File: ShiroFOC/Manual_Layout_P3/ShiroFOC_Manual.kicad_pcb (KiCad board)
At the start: 6 copper layers, 45 x 45 mm, 266 parts, among them J1 Motor phases - solder wires, J1001 TC2030-NL SWD, J101 DC input - solder wires, J201 USB-C service, J501 BRAKE RESISTOR, J502 5V PWM FAN, J601 EXT ENCODER / HALL, J801 CAN 1, J802 CAN 2, Q201 CSD17483F4, Q301 CSD17483F4, Q501 ISZ080N10NM6 100V, Q801 CSD17483F4, Q802 CSD87502Q2, U1 CSD88599Q5DC, U2 CSD88599Q5DC, U201 LMR36510FADDAR, U202 USBLC6-2SC6, U203 TPS2121RUXR, U204 TLV75533PDYDR, U205 MPM3620AGQV-Z, U3 CSD88599Q5DC, U4 STSPIN32G4, U501 UCC27517ADBVR, U502 TLV3012BIDCKR, U503 74AHCT1G125W5-7, U601 AS5047P-ATSM, U602 TMUX1574PW, U603 74LVC3G17, U604 TPS2553DBVR, U701 BMI323, U801 TCAN3413DRBR, U901 CP2102N-A02-GQFN20, Y301 24MHz 7pF

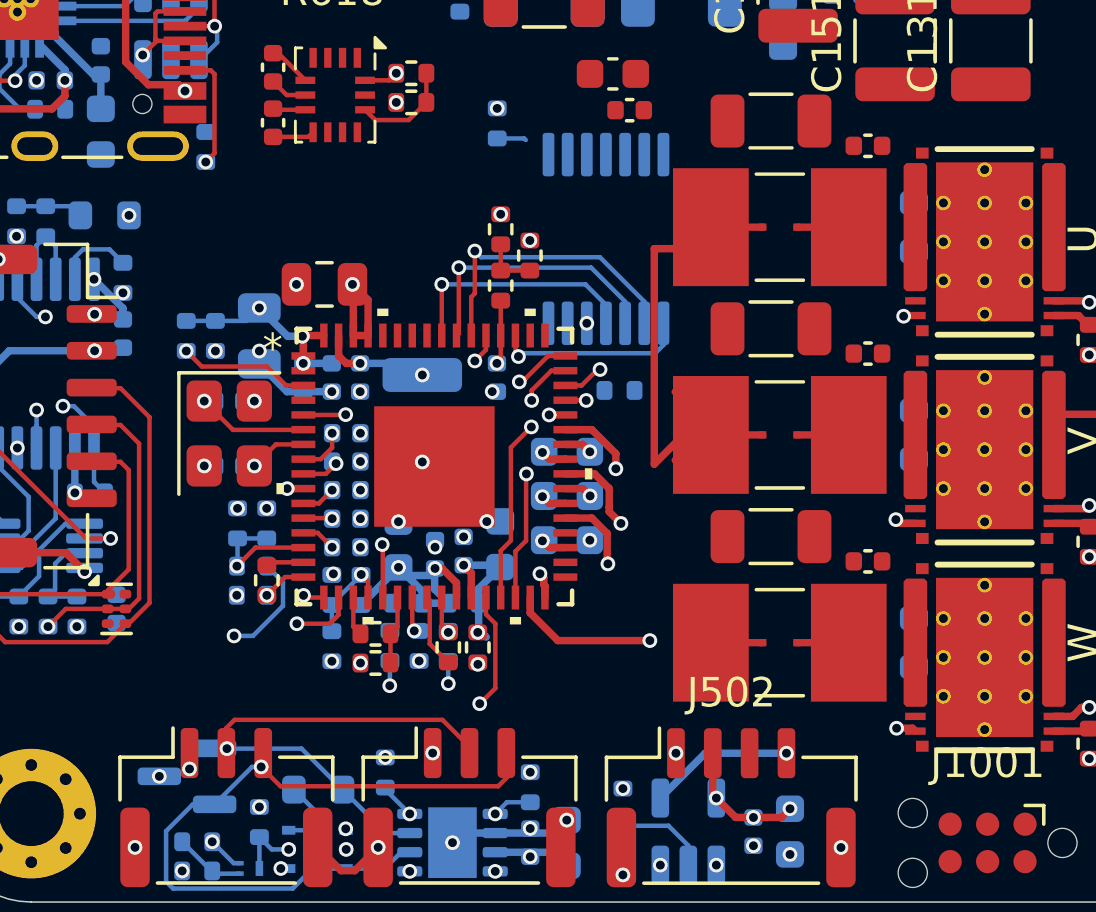
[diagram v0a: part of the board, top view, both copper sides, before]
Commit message: op amp traces draft
swapped phase U and W op amps
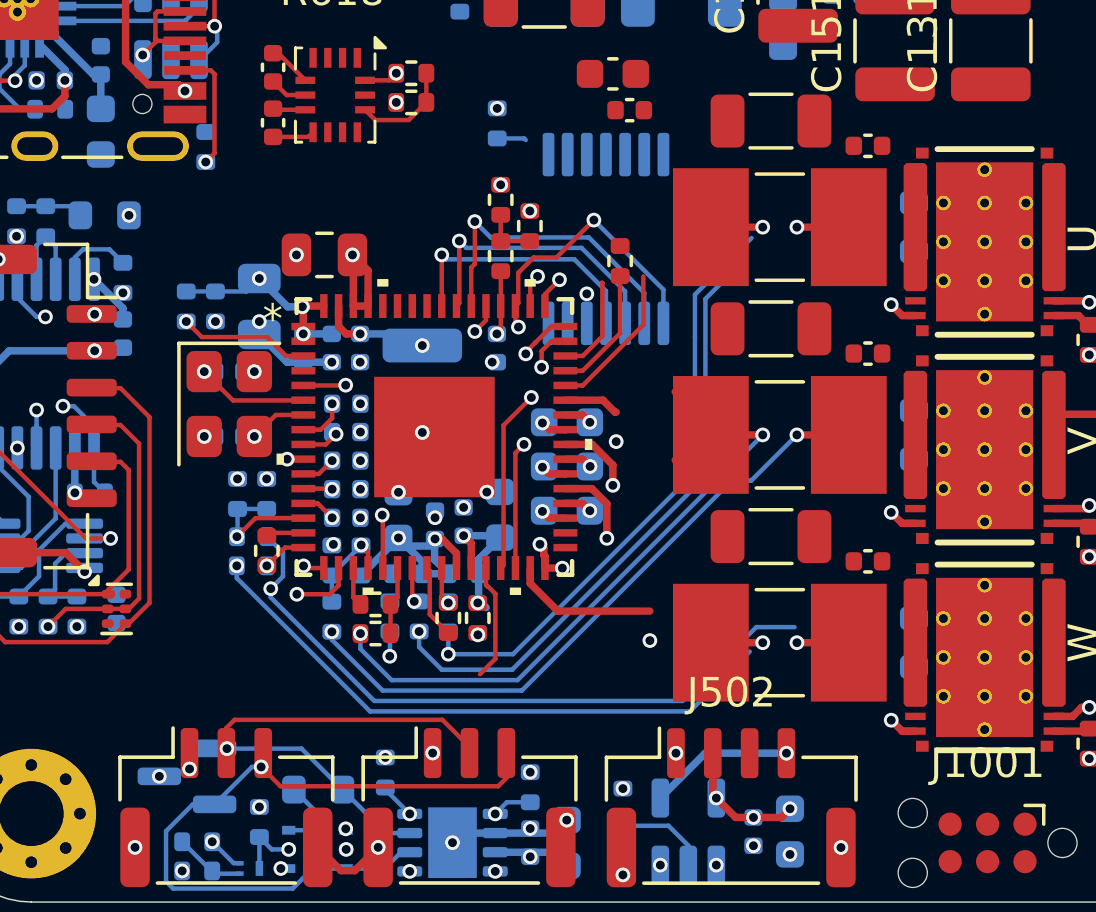
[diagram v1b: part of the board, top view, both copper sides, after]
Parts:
- R903: moved to F.Cu
- moved R903 4.39 mm to (0.48, 0.75), turned to 90 degrees
- moved C108 1.00 mm to (-8.81, 6.55)
- moved C12 1.00 mm to (-1.32, 9.22)
- moved C301 1.00 mm to (-10.3, 3.70)
- moved C302 1.00 mm to (-11.8, 2.29)
- moved C303 1.00 mm to (-4.83, 9.59)
- moved C304 1.00 mm to (-3.59, 9.36)
- moved C305 1.00 mm to (-5.80, 9.70)
- moved C306 1.00 mm to (-7.04, 9.37)
- moved C307 1.00 mm to (-9.30, 3.70)
- moved C308 1.00 mm to (-12.8, 4.50)
- moved C309 1.00 mm to (-12.8, 6.70)
- moved C310 1.00 mm to (-8.81, 5.59)
- moved C311 1.00 mm to (-9.55, 0.54)
- moved C312 1.00 mm to (-6.23, 5.09)
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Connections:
- R410 pad 2: /Current / temperature/OPP_U1 -> /Current / temperature/OPP_W1
- R417 pad 1: SHUNT_U_SENSE_P -> SHUNT_W_SENSE_P
- R417 pad 2: /Current / temperature/OPP_U1 -> /Current / temperature/OPP_W1
- R418 pad 1: SHUNT_U_SENSE_N -> SHUNT_W_SENSE_N
- R418 pad 2: /Current / temperature/OPN_U1 -> /Current / temperature/OPN_W1
- R419 pad 1: OPO_U1 -> OPO_W1
- R419 pad 2: /Current / temperature/OPN_U1 -> /Current / temperature/OPN_W1
- R430 pad 2: /Current / temperature/OPP_W1 -> /Current / temperature/OPP_U1
- R437 pad 1: SHUNT_W_SENSE_P -> SHUNT_U_SENSE_P
- R437 pad 2: /Current / temperature/OPP_W1 -> /Current / temperature/OPP_U1
- R438 pad 1: SHUNT_W_SENSE_N -> SHUNT_U_SENSE_N
- R438 pad 2: /Current / temperature/OPN_W1 -> /Current / temperature/OPN_U1
- R439 pad 1: OPO_W1 -> OPO_U1
- R439 pad 2: /Current / temperature/OPN_W1 -> /Current / temperature/OPN_U1
- R441 pad 1: /Current / temperature/OPP_U1 -> /Current / temperature/OPP_W1
- R443 pad 1: /Current / temperature/OPP_W1 -> /Current / temperature/OPP_U1
- U4 pad 14: /Current / temperature/OPP_U1 -> /Current / temperature/OPP_W1
- U4 pad 15: OPO_U1 -> OPO_W1
- U4 pad 16: /Current / temperature/OPN_U1 -> /Current / temperature/OPN_W1
- U4 pad 23: /Current / temperature/OPP_W1 -> /Current / temperature/OPP_U1
- U4 pad 24: OPO_W1 -> OPO_U1
- U4 pad 25: /Current / temperature/OPN_W1 -> /Current / temperature/OPN_U1
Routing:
- net SHUNT_W_SENSE_P: track 0.00 -> 22.7 mm, vias 1 -> 2
- net SHUNT_U_SENSE_N: track 0.00 -> 20.4 mm, vias 1 -> 2
- net SHUNT_V_SENSE_P: track 0.00 -> 20.4 mm, vias 1 -> 2
- net SHUNT_W_SENSE_N: track 0.77 -> 20.5 mm, vias 1 -> 2
- net SHUNT_V_SENSE_N: track 0.00 -> 18.1 mm, vias 1 -> 2
- net SHUNT_U_SENSE_P: track 3.66 -> 20.7 mm, vias 1 -> 2
- net GND: track 59.4 -> 48.1 mm, vias 55 -> 56
- net USB_UART_TX: track 0.71 -> 4.32 mm, vias 1 -> 0
- net AS5047P_CS_N: track 7.77 -> 11.1 mm, vias 1 -> 2
- net /Current / temperature/OPP_W1: track 1.16 -> 4.45 mm
- net /Current / temperature/OPP_U1: track 4.45 -> 1.16 mm
- net USB_UART_RX: track 8.09 -> 10.0 mm, vias 2 -> 1
- net I2C2_SDA: track 15.5 -> 13.6 mm, vias 2 -> 1
- net FDCAN1_TX: track 16.8 -> 15.4 mm
- net OPO_W1: track 2.50 -> 1.28 mm
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
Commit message: shunts updated
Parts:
- removed C126: 10uF DNP, Capacitor_SMD:C_1210_3225Metric
- added C_PREVIEW_BULK1: 680uF 63V - placement preview, ShiroFOCLib:Panasonic_EEVFK_K16_18x16.5, F.Cu at (-24.0, 61.5)
- added C_PREVIEW_BULK2: 680uF 63V - placement preview, ShiroFOCLib:Panasonic_EEVFK_K16_18x16.5, F.Cu at (0.00, 61.5)
- added C_PREVIEW_BULK3: 680uF 63V - placement preview, ShiroFOCLib:Panasonic_EEVFK_K16_18x16.5, F.Cu at (23.6, 62.8)
- added SW301: RESET, Button_Switch_SMD:SW_Push_1P1T-SH_NO_CK_KMR2xxG, F.Cu at (-33.7, -8.25)
- C101, C102, C11, C110, C111, C112, C113, C127, C128, C129, C144, C145, C149, C154, C3, C7: moved to B.Cu
- R1, R3, R5: footprint ShiroFOCLib:R_Shunt_LR2512D_0m5_3W_Kelvin -> ShiroFOCLib:R_Shunt_HCS1206_0m5_2W_Kelvin
- moved C3 63.3 mm to (9.21, 4.65), turned to 180 degrees
- moved C7 62.8 mm to (9.22, 7.90), turned to 180 degrees
- moved C11 62.3 mm to (9.22, 11.1), turned to 180 degrees
- moved C149 58.3 mm to (13.9, -5.06)
- moved C127 58.1 mm to (9.23, 14.4), turned to 180 degrees
- moved C111 54.0 mm to (13.9, 17.7)
- moved C101 53.4 mm to (9.21, 17.6), turned to 180 degrees
- moved C145 50.1 mm to (13.8, 4.70)
- moved C144 48.9 mm to (13.9, -1.80)
- moved C129 48.9 mm to (13.9, 14.4)
- moved C154 46.5 mm to (13.8, 1.45)
- moved C128 44.7 mm to (9.23, -5.05), turned to 180 degrees
- moved C113 42.6 mm to (13.9, 11.2)
- moved C112 41.0 mm to (9.23, -1.81), turned to 180 degrees
- moved C102 38.2 mm to (9.22, 1.41), turned to 180 degrees
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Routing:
- net GHS3: track 23.7 -> 1.62 mm, vias 2 -> 1
- net HS_RETURN_W: track 24.5 -> 2.73 mm
- net FEEDBACK_A_H1: track 1.44 -> 21.6 mm
- net HS_RETURN_U: track 21.5 -> 2.66 mm
- net FEEDBACK_B_H2: track 1.29 -> 18.9 mm
- net GHS1: track 19.4 -> 2.07 mm
- net GHS2: track 19.3 -> 2.82 mm
- net HS_RETURN_V: track 20.2 -> 3.68 mm
- net FEEDBACK_I_H3: track 1.70 -> 18.0 mm
- net USB_UART_RX: track 10.0 -> 22.4 mm, vias 1 -> 2
- net /USB service/UART_BRIDGE_RX: track 12.8 -> 23.8 mm, vias 1 -> 2
- net GLS1: track 21.3 -> 16.3 mm
- net VBUS_SENSE: track 9.49 -> 14.4 mm
- net GLS3: track 14.6 -> 10.3 mm, vias 2 -> 1
- net I2C2_SDA: track 13.6 -> 10.4 mm
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
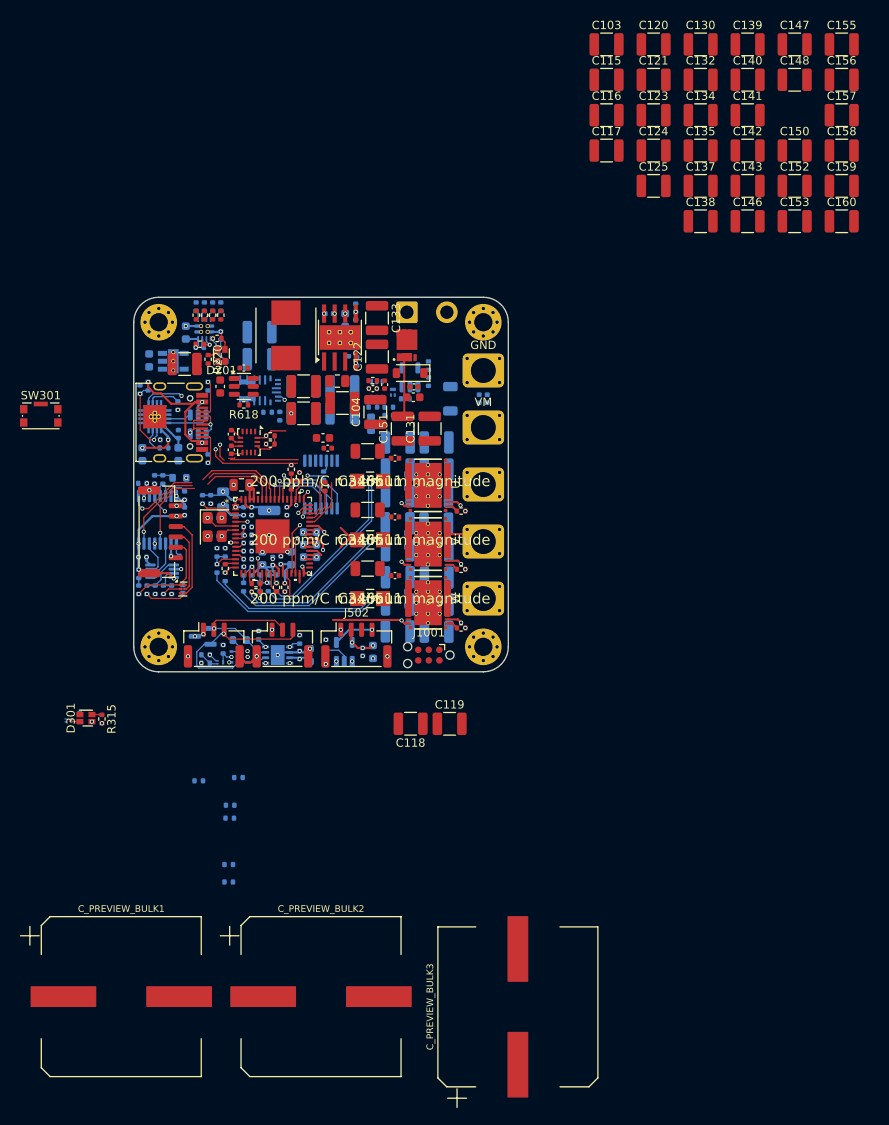
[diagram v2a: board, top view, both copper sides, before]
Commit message: mosfet stages and opamps revamped
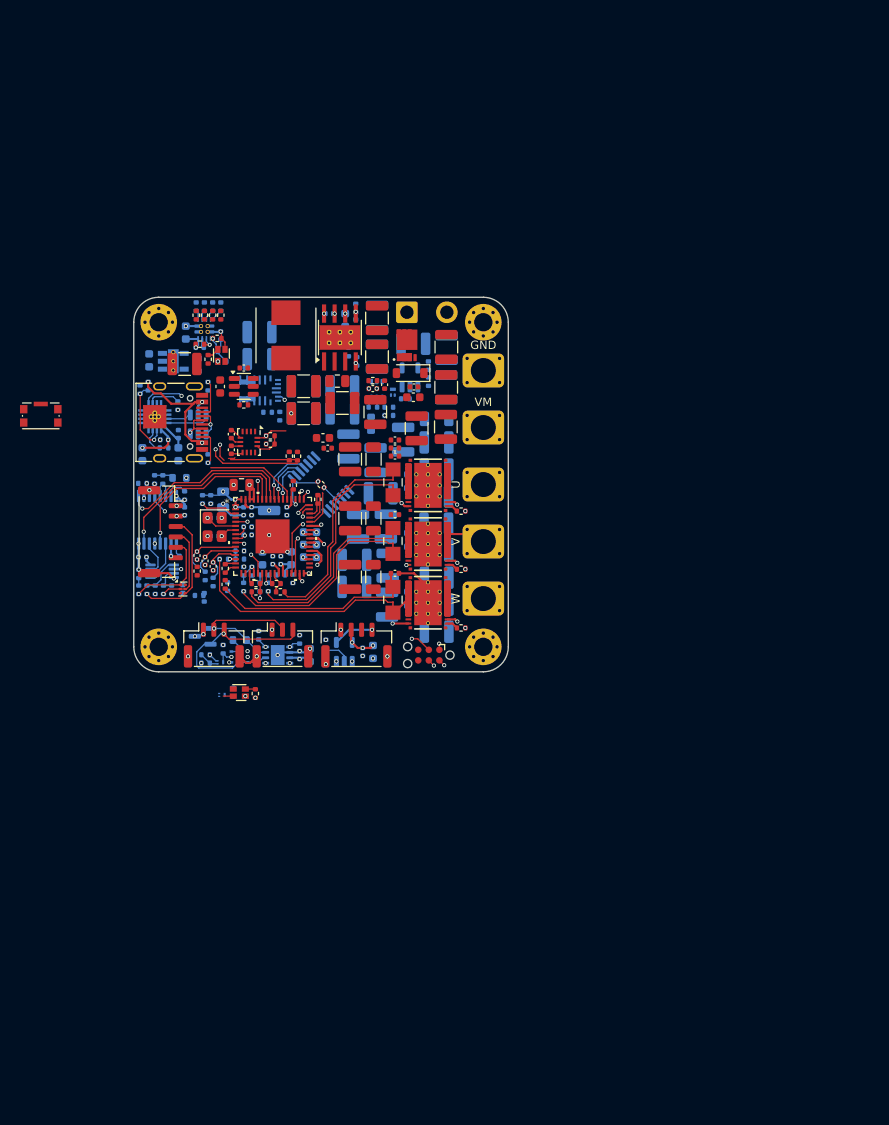
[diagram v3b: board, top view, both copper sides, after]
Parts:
- removed C103, C115, C118, C119, C120, C121, C130, C132, C139, C140, C141, C147, C148, C155, C156, C157, C158: 10uF, Capacitor_SMD:C_1210_3225Metric
- removed C125, C142, C143, C159, C160: 10uF DNP, Capacitor_SMD:C_1210_3225Metric
- removed C_PREVIEW_BULK1, C_PREVIEW_BULK2, C_PREVIEW_BULK3: 680uF 63V - placement preview, ShiroFOCLib:Panasonic_EEVFK_K16_18x16.5
- C105, C106, C711, C712, C713, R309, R418, R438, R712: moved to F.Cu
- C11, C3, C7: value 4.7uF -> 10uF; moved to F.Cu
- C116, C123, C134, C135, C137, C138, C146, C150, C152, C153, R301: moved to B.Cu
- moved C152 70.2 mm to (7.94, 14.4), turned to -90 degrees
- moved C153 61.3 mm to (7.79, 5.05), turned to -90 degrees
- moved C137 59.1 mm to (8.01, 9.74), turned to 90 degrees
- moved C146 53.1 mm to (6.55, -2.92), turned to -90 degrees
- moved C150 51.4 mm to (11.1, -16.9), turned to 180 degrees
- moved C134 48.5 mm to (6.73, -15.4), turned to 90 degrees
- moved C138 44.3 mm to (9.87, -5.40), turned to 90 degrees
- moved C135 41.8 mm to (15.0, -11.7), turned to 90 degrees
- moved C123 41.2 mm to (6.74, -20.1), turned to -90 degrees
- moved C124 37.8 mm to (15.0, -11.7), turned to 90 degrees
- moved R703 35.5 mm to (-11.2, 12.3), turned to -90 degrees
- moved C116 33.9 mm to (15.1, -16.4), turned to -90 degrees
- moved R702 32.5 mm to (-14.6, 13.3), turned to 180 degrees
- moved C117 30.5 mm to (15.1, -16.5), turned to -90 degrees
- moved R712 29.9 mm to (-14.9, 10.4), turned to 90 degrees
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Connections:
- U602 pad 4: FEEDBACK_B_H2 -> FEEDBACK_I_H3
- U602 pad 7: FEEDBACK_A_H1 -> FEEDBACK_B_H2
- U602 pad 9: FEEDBACK_I_H3 -> FEEDBACK_A_H1
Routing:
- net GHS3: track 1.62 -> 24.3 mm, vias 1 -> 2
- net BRAKE_PWM: track 0.00 -> 20.7 mm, vias 0 -> 2
- net HS_RETURN_W: track 2.73 -> 22.9 mm
- net HS_RETURN_U: track 2.66 -> 21.3 mm
- net GHS2: track 2.82 -> 20.7 mm
- net HS_RETURN_V: track 3.68 -> 21.3 mm
- net GHS1: track 2.07 -> 19.5 mm
- net GND: track 48.0 -> 30.8 mm, vias 56 -> 53
- net EXT_FEEDBACK_SELECT: track 1.68 -> 13.0 mm
- net /USB service/UART_BRIDGE_RX: track 23.8 -> 14.9 mm
- net Net-(R310-Pad2): track 1.88 -> 8.93 mm
- net VREF+: track 8.20 -> 1.48 mm, vias 3 -> 1
- net VM: track 5.94 -> 12.0 mm
- net SPI3_SCK_MCU: track 10.7 -> 4.78 mm
- net GLS3: track 10.3 -> 16.0 mm, vias 1 -> 2
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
